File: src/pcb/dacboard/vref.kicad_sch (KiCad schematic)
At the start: 48 parts, among them J1 Screw_Terminal_01x03, J2 Screw_Terminal_01x02, U1 LTC6655CHMS8-2.5_PBF, U2 LTC6655CHMS8-2.5_PBF, U3 LTC6655CHMS8-2.5_PBF, U4 LTC6655CHMS8-2.5_PBF, U5 LTC6655CHMS8-2.5_PBF, U6 LTC6655CHMS8-2.5_PBF, U7 LTC6655CHMS8-2.5_PBF, U8 LTC6655CHMS8-2.5_PBF, U9 AD8676xR

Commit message: dacboard routing
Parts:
- C1, C11, C13, C15, C3, C5, C7, C9: footprint (none) -> Capacitor_SMD:C_0402_1005Metric_Pad0.74x0.62mm_HandSolder
- C10, C12, C14, C16, C2, C4, C6, C8: footprint (none) -> Capacitor_SMD:C_0603_1608Metric_Pad1.08x0.95mm_HandSolder
- C17, C18, C19, C20, C21: footprint (none) -> Capacitor_SMD:C_0805_2012Metric
- J1: footprint (none) -> TerminalBlock_Phoenix:TerminalBlock_Phoenix_MKDS-1,5-3-5.08_1x03_P5.08mm_Horizontal
- J2: footprint (none) -> TerminalBlock_4Ucon:TerminalBlock_4Ucon_1x02_P3.50mm_Horizontal
- R1, R2, R3, R4, R5, R6, R7, R8: footprint (none) -> Resistor_SMD:R_0805_2012Metric_Pad1.20x1.40mm_HandSolder
- R10, R9: footprint LT5400BCMS8E-7_PBF:SOP65P490X110-9N -> Package_SO:MSOP-8-1EP_3x3mm_P0.65mm_EP1.68x1.88mm
- R11, R12, R13, R14: footprint (none) -> Resistor_SMD:R_0805_2012Metric
- R15, R40: footprint (none) -> Resistor_THT:R_Axial_DIN0309_L9.0mm_D3.2mm_P12.70mm_Horizontal
- U1, U2, U3, U4, U5, U6, U7, U8: footprint LTC6655CHMS8-2.5_PBF:SOP65P490X110-8N -> Package_LCC:Analog_LCC-8_5x5mm_P1.27mm
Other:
- moved on the sheet: J2

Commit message: analog side layout
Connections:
- net AGND: now also U9.5 (+); no longer U9.3 (+)
- net at C17.1, R1.2, R2.2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: now also U9.3 (+); no longer U9.5 (+)
- net at R10.1, R10.2: now also U9.2 (-); no longer U9.6 (-)
- net at R10.8, R13.1: now also U9.1; no longer U9.7
- net at R11.1, R9.8: now also U9.7; no longer U9.1
- net at R9.1, R9.2, R9.3: now also U9.6 (-); no longer U9.2 (-)
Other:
- moved on the sheet: U9A, U9B
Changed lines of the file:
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@@
 	)
 	(junction
+		(at 224.79 85.09)
+		(diameter 0)
+		(color 0 0 0 0)
+	)
+	(junction
 		(at 184.15 127)
 		(diameter 0)
@@
 	)
 	(junction
-		(at 224.79 129.54)
-		(diameter 0)
-		(color 0 0 0 0)
-	)
-	(junction
 		(at 30.48 52.07)
 		(diameter 0)
@@
 	)
 	(junction
-		(at 224.79 85.09)
-		(diameter 0)
-		(color 0 0 0 0)
-	)
-	(junction
 		(at 133.35 156.21)
 		(diameter 0)
@@
 	)
 	(junction
+		(at 224.79 129.54)
+		(diameter 0)
+		(color 0 0 0 0)
+	)
+	(junction
 		(at 138.43 114.3)
 		(diameter 0)
@@
 	(wire
 		(pts
-			(xy 196.85 87.63) (xy 201.93 87.63)
-		)
-		(stroke
-			(width 0)
-			(type default)
-		)
-	)
-	(wire
-		(pts
 			(xy 87.63 138.43) (xy 97.79 138.43)
 		)
@@
 	(wire
 		(pts
+			(xy 196.85 132.08) (xy 203.2 132.08)
+		)
+		(stroke
+			(width 0)
+			(type default)
+		)
+	)
+	(wire
+		(pts
 			(xy 133.35 119.38) (xy 133.35 121.92)
 		)
@@
 	(wire
 		(pts
-			(xy 201.93 132.08) (xy 196.85 132.08)
-		)
-		(stroke
-			(width 0)
-			(type default)
-		)
-	)
-	(wire
-		(pts
 			(xy 184.15 82.55) (xy 184.15 91.44)
 		)
@@
 	(wire
 		(pts
-			(xy 184.15 127) (xy 201.93 127)
-		)
-		(stroke
-			(width 0)
-			(type default)
-		)
-	)
-	(wire
-		(pts
 			(xy 184.15 109.22) (xy 184.15 115.57)
 		)
@@
 	(wire
 		(pts
-			(xy 217.17 85.09) (xy 224.79 85.09)
-		)
-		(stroke
-			(width 0)
-			(type default)
-		)
-	)
-	(wire
-		(pts
 			(xy 71.12 113.03) (xy 66.04 113.03)
 		)
@@
 	(wire
 		(pts
+			(xy 218.44 85.09) (xy 224.79 85.09)
+		)
+		(stroke
+			(width 0)
+			(type default)
+		)
+	)
+	(wire
+		(pts
 			(xy 66.04 87.63) (xy 66.04 90.17)
 		)
@@
 	(wire
 		(pts
+			(xy 196.85 87.63) (xy 203.2 87.63)
+		)
+		(stroke
+			(width 0)
+			(type default)
+		)
+	)
+	(wire
+		(pts
 			(xy 30.48 107.95) (xy 30.48 113.03)
 		)
@@
 	(wire
 		(pts
-			(xy 224.79 99.06) (xy 219.71 99.06)
+			(xy 184.15 127) (xy 203.2 127)
 		)
 		(stroke
@@
 	(wire
 		(pts
-			(xy 71.12 46.99) (xy 72.39 46.99)
+			(xy 224.79 99.06) (xy 219.71 99.06)
 		)
 		(stroke
@@
 	(wire
 		(pts
-			(xy 20.32 46.99) (xy 30.48 46.99)
+			(xy 71.12 46.99) (xy 72.39 46.99)
 		)
 		(stroke
@@
 	(wire
 		(pts
-			(xy 224.79 129.54) (xy 217.17 129.54)
+			(xy 218.44 129.54) (xy 224.79 129.54)
 		)
 		(stroke
@@
 	(wire
 		(pts
-			(xy 224.79 102.87) (xy 224.79 115.57)
+			(xy 20.32 46.99) (xy 30.48 46.99)
 		)
 		(stroke
@@
 	(wire
 		(pts
-			(xy 193.04 82.55) (xy 201.93 82.55)
+			(xy 224.79 102.87) (xy 224.79 115.57)
 		)
 		(stroke
@@
 	(wire
 		(pts
+			(xy 193.04 82.55) (xy 203.2 82.55)
+		)
+		(stroke
+			(width 0)
+			(type default)
+		)
+	)
+	(wire
+		(pts
 			(xy 87.63 77.47) (xy 97.79 77.47)
 		)
@@
 	(symbol
 		(lib_id "Amplifier_Operational:AD8676xR")
-		(at 209.55 129.54 0)
+		(at 210.82 85.09 0)
 		(unit 2)
 		(exclude_from_sim no)
@@
 		(fields_autoplaced yes)
 		(property "Reference" "U9"
-			(at 209.55 119.38 0)
+			(at 210.82 74.93 0)
 			(effects
 				(font
@@
 		)
 		(property "Value" "AD8676xR"
-			(at 209.55 121.92 0)
+			(at 210.82 77.47 0)
 			(effects
 				(font
@@
 		)
 		(property "Footprint" "Package_SO:SOIC-8_3.9x4.9mm_P1.27mm"
-			(at 212.09 129.54 0)
+			(at 213.36 85.09 0)
 			(effects
 				(font
@@
 		)
 		(property "Datasheet" "https://www.analog.com/media/en/technical-documentation/data-sheets/AD8676.pdf"
-			(at 215.9 125.73 0)
+			(at 217.17 81.28 0)
 			(effects
 				(font
@@
 		)
 		(property "Description" "Dual operational amplifier, Ultra-precision, 36V, Rail-to-rail output, SOIC-8"
-			(at 209.55 129.54 0)
+			(at 210.82 85.09 0)
 			(effects
 				(font
@@
 	(symbol
 		(lib_id "Amplifier_Operational:AD8676xR")
-		(at 209.55 85.09 0)
+		(at 210.82 129.54 0)
 		(unit 1)
 		(exclude_from_sim no)
@@
 		(fields_autoplaced yes)
 		(property "Reference" "U9"
-			(at 209.55 74.93 0)
+			(at 210.82 119.38 0)
 			(effects
 				(font
@@
 		)
 		(property "Value" "AD8676xR"
-			(at 209.55 77.47 0)
+			(at 210.82 121.92 0)
 			(effects
 				(font
@@
 		)
 		(property "Footprint" "Package_SO:SOIC-8_3.9x4.9mm_P1.27mm"
-			(at 212.09 85.09 0)
+			(at 213.36 129.54 0)
 			(effects
 				(font
@@
 		)
 		(property "Datasheet" "https://www.analog.com/media/en/technical-documentation/data-sheets/AD8676.pdf"
-			(at 215.9 81.28 0)
+			(at 217.17 125.73 0)
 			(effects
 				(font
@@
 		)
 		(property "Description" "Dual operational amplifier, Ultra-precision, 36V, Rail-to-rail output, SOIC-8"
-			(at 209.55 85.09 0)
+			(at 210.82 129.54 0)
 			(effects
 				(font

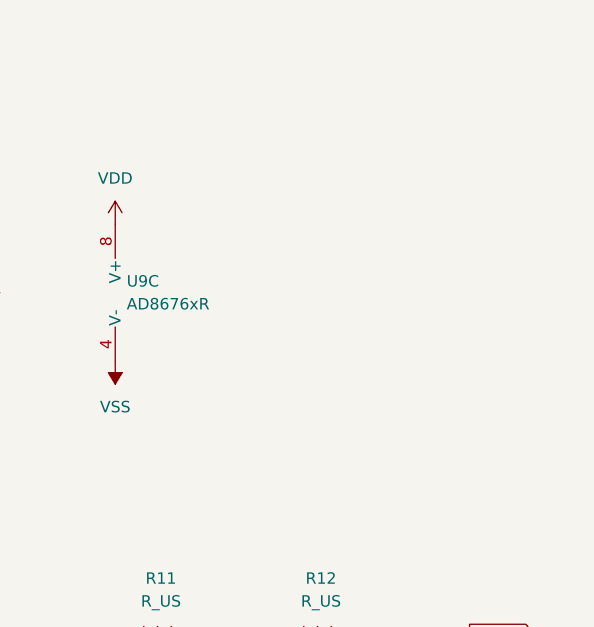
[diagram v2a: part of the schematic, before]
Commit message: low noise digital finished
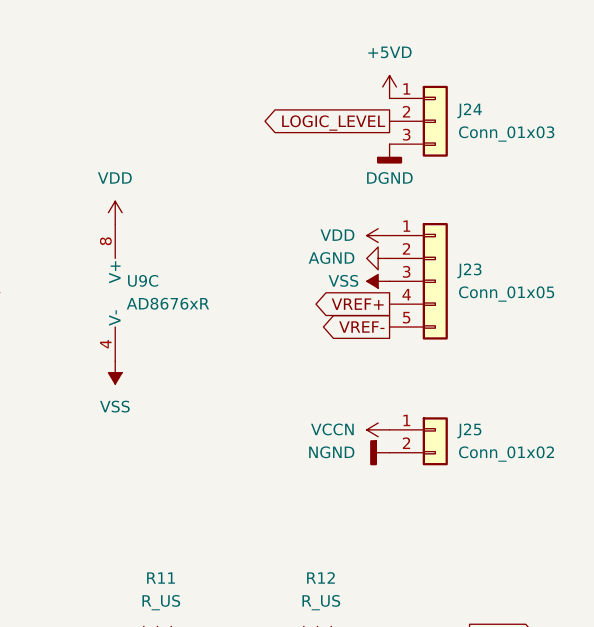
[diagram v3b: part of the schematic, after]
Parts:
- added J23: Conn_01x05, Connector_PinHeader_2.54mm:PinHeader_1x05_P2.54mm_Vertical, symbol Connector_Generic:Conn_01x05
- added J24: Conn_01x03, Connector_PinHeader_2.54mm:PinHeader_1x03_P2.54mm_Vertical, symbol Connector_Generic:Conn_01x03
- added J25: Conn_01x02, Connector_PinHeader_2.54mm:PinHeader_1x02_P2.54mm_Vertical, symbol Connector_Generic:Conn_01x02
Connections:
- net +5VD: now also J24.1 (Pin_1)
- net AGND: now also J23.2 (Pin_2)
- net DGND: now also J24.3 (Pin_3)
- net LOGIC_LEVEL: now also J24.2 (Pin_2)
- net VDD: now also J23.1 (Pin_1)
- net VREF+: now also J23.4 (Pin_4)
- net VREF-: now also J23.5 (Pin_5)
- net VSS: now also J23.3 (Pin_3)
- new net NGND: J25.2 (Pin_2)
- new net VCCN: J25.1 (Pin_1)

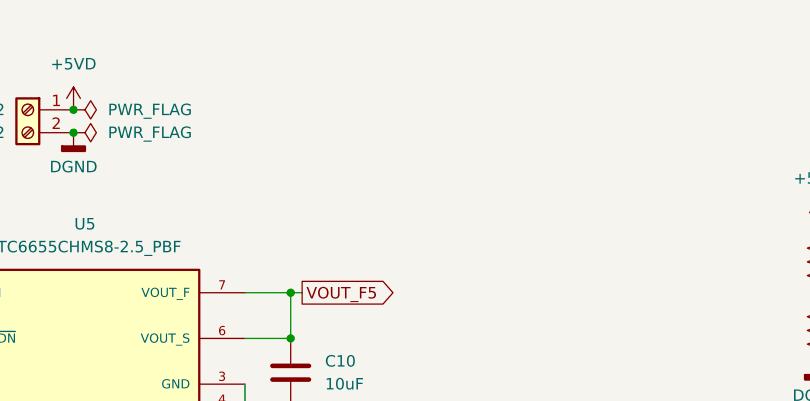
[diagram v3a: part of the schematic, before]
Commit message: finished routing fpga connections
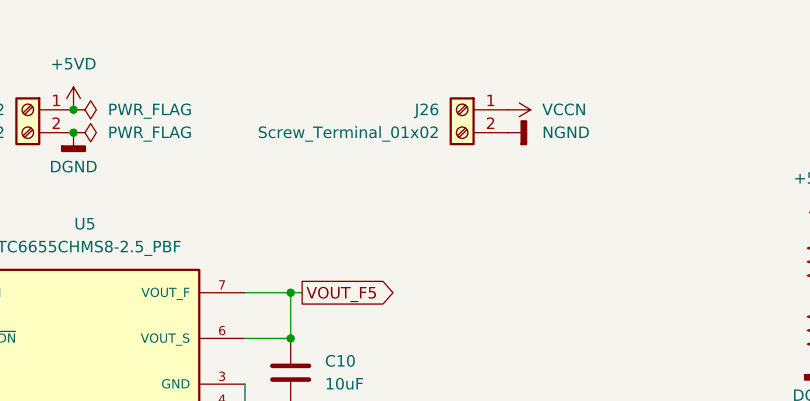
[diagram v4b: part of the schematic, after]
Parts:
- added J26: Screw_Terminal_01x02, TerminalBlock_4Ucon:TerminalBlock_4Ucon_1x02_P3.50mm_Horizontal, symbol Connector:Screw_Terminal_01x02
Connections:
- net NGND: now also J26.2 (Pin_2)
- net VCCN: now also J26.1 (Pin_1)
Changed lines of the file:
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@@
 	)
 	(symbol
+		(lib_id "power:GNDD")
+		(at 162.56 29.21 90)
+		(unit 1)
+		(exclude_from_sim no)
+		(in_bom yes)
+		(on_board yes)
+		(dnp no)
+		(fields_autoplaced yes)
+		(property "Reference" "#PWR0509"
+			(at 168.91 29.21 0)
+			(effects
+				(font
+					(size 1.27 1.27)
+				)
+				(hide yes)
+			)
+		)
+		(property "Value" "NGND"
+			(at 166.37 29.2099 90)
+			(effects
+				(font
+					(size 1.27 1.27)
+				)
+				(justify right)
+			)
+		)
+		(property "Footprint" ""
+			(at 162.56 29.21 0)
+			(effects
+				(font
+					(size 1.27 1.27)
+				)
+				(hide yes)
+			)
+		)
+		(property "Datasheet" ""
+			(at 162.56 29.21 0)
+			(effects
+				(font
+					(size 1.27 1.27)
+				)
+				(hide yes)
+			)
+		)
+		(property "Description" "Power symbol creates a global label with name \"GNDD\" , digital ground"
+			(at 162.56 29.21 0)
+			(effects
+				(font
+					(size 1.27 1.27)
+				)
+				(hide yes)
+			)
+		)
+		(pin "1"
+		)
+		(instances
+			(project "dacboard"
+				(path "/35cb74e4-0f64-454b-9b50-bfac13ed28a5/40dec0c3-ad5f-493b-813b-faaee90d807a"
+					(reference "#PWR0509")
+					(unit 1)
+				)
+			)
+		)
+	)
+	(symbol
 		(lib_id "power:GND")
 		(at 138.43 121.92 0)
@@
 	)
 	(symbol
+		(lib_id "power:VCC")
+		(at 162.56 26.67 270)
+		(mirror x)
+		(unit 1)
+		(exclude_from_sim no)
+		(in_bom yes)
+		(on_board yes)
+		(dnp no)
+		(property "Reference" "#PWR0508"
+			(at 158.75 26.67 0)
+			(effects
+				(font
+					(size 1.27 1.27)
+				)
+				(hide yes)
+			)
+		)
+		(property "Value" "VCCN"
+			(at 166.37 26.6699 90)
+			(effects
+				(font
+					(size 1.27 1.27)
+				)
+				(justify left)
+			)
+		)
+		(property "Footprint" ""
+			(at 162.56 26.67 0)
+			(effects
+				(font
+					(size 1.27 1.27)
+				)
+				(hide yes)
+			)
+		)
+		(property "Datasheet" ""
+			(at 162.56 26.67 0)
+			(effects
+				(font
+					(size 1.27 1.27)
+				)
+				(hide yes)
+			)
+		)
+		(property "Description" "Power symbol creates a global label with name \"VCC\""
+			(at 162.56 26.67 0)
+			(effects
+				(font
+					(size 1.27 1.27)
+				)
+				(hide yes)
+			)
+		)
+		(pin "1"
+		)
+		(instances
+			(project "dacboard"
+				(path "/35cb74e4-0f64-454b-9b50-bfac13ed28a5/40dec0c3-ad5f-493b-813b-faaee90d807a"
+					(reference "#PWR0508")
+					(unit 1)
+				)
+			)
+		)
+	)
+	(symbol
 		(lib_id "power:GND")
 		(at 66.04 95.25 0)
@@
 					(unit 1)
 				)
+			)
+		)
+	)
+	(symbol
+		(lib_id "Connector:Screw_Terminal_01x02")
+		(at 157.48 26.67 0)
+		(mirror y)
+		(unit 1)
+		(exclude_from_sim no)
+		(in_bom yes)
+		(on_board yes)
+		(dnp no)
+		(property "Reference" "J26"
+			(at 154.94 26.6699 0)
+			(effects
+				(font
+					(size 1.27 1.27)
+				)
+				(justify left)
+			)
+		)
+		(property "Value" "Screw_Terminal_01x02"
+			(at 154.94 29.2099 0)
+			(effects
+				(font
+					(size 1.27 1.27)
+				)
+				(justify left)
+			)
+		)
+		(property "Footprint" "TerminalBlock_4Ucon:TerminalBlock_4Ucon_1x02_P3.50mm_Horizontal"
+			(at 157.48 26.67 0)
+			(effects
+				(font
+					(size 1.27 1.27)
+				)
+				(hide yes)
+			)
+		)
+		(property "Datasheet" "~"
+			(at 157.48 26.67 0)
+			(effects
+				(font
+					(size 1.27 1.27)
+				)
+				(hide yes)
+			)
+		)
+		(property "Description" "Generic screw terminal, single row, 01x02, script generated (kicad-library-utils/schlib/autogen/connector/)"
+			(at 157.48 26.67 0)
+			(effects
+				(font
+					(size 1.27 1.27)
+				)
+				(hide yes)
+			)
+		)
+		(pin "1"
+		)
+		(pin "2"
+		)
+		(instances
+			(project "dacboard"
+				(path "/35cb74e4-0f64-454b-9b50-bfac13ed28a5/40dec0c3-ad5f-493b-813b-faaee90d807a"
+					(reference "J26")
+					(unit 1)
+				)

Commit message: dacboard finished
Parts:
- added R41: R_US, Resistor_THT:R_Axial_DIN0309_L9.0mm_D3.2mm_P20.32mm_Horizontal, symbol Device:R_US
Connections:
- net AGND: now also R41.1
- net DGND: now also R41.2
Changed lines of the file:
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@@
 	(symbol
 		(lib_id "Device:R_US")
+		(at 165.1 46.99 0)
+		(unit 1)
+		(exclude_from_sim no)
+		(in_bom yes)
+		(on_board yes)
+		(dnp no)
+		(fields_autoplaced yes)
+		(property "Reference" "R41"
+			(at 167.64 45.7199 0)
+			(effects
+				(font
+					(size 1.27 1.27)
+				)
+				(justify left)
+			)
+		)
+		(property "Value" "R_US"
+			(at 167.64 48.2599 0)
+			(effects
+				(font
+					(size 1.27 1.27)
+				)
+				(justify left)
+			)
+		)
+		(property "Footprint" "Resistor_THT:R_Axial_DIN0309_L9.0mm_D3.2mm_P20.32mm_Horizontal"
+			(at 166.116 47.244 90)
+			(effects
+				(font
+					(size 1.27 1.27)
+				)
+				(hide yes)
+			)
+		)
+		(property "Datasheet" "~"
+			(at 165.1 46.99 0)
+			(effects
+				(font
+					(size 1.27 1.27)
+				)
+				(hide yes)
+			)
+		)
+		(property "Description" "Resistor, US symbol"
+			(at 165.1 46.99 0)
+			(effects
+				(font
+					(size 1.27 1.27)
+				)
+				(hide yes)
+			)
+		)
+		(pin "1"
+		)
+		(pin "2"
+		)
+		(instances
+			(project ""
+				(path "/35cb74e4-0f64-454b-9b50-bfac13ed28a5/40dec0c3-ad5f-493b-813b-faaee90d807a"
+					(reference "R41")
+					(unit 1)
+				)
+			)
+		)
+	)
+	(symbol
+		(lib_id "Device:R_US")
 		(at 180.34 127 90)
 		(unit 1)
@@
 	)
 	(symbol
+		(lib_id "power:GNDD")
+		(at 165.1 50.8 0)
+		(unit 1)
+		(exclude_from_sim no)
+		(in_bom yes)
+		(on_board yes)
+		(dnp no)
+		(fields_autoplaced yes)
+		(property "Reference" "#PWR0542"
+			(at 165.1 57.15 0)
+			(effects
+				(font
+					(size 1.27 1.27)
+				)
+				(hide yes)
+			)
+		)
+		(property "Value" "DGND"
+			(at 165.1 54.61 0)
+			(effects
+				(font
+					(size 1.27 1.27)
+				)
+			)
+		)
+		(property "Footprint" ""
+			(at 165.1 50.8 0)
+			(effects
+				(font
+					(size 1.27 1.27)
+				)
+				(hide yes)
+			)
+		)
+		(property "Datasheet" ""
+			(at 165.1 50.8 0)
+			(effects
+				(font
+					(size 1.27 1.27)
+				)
+				(hide yes)
+			)
+		)
+		(property "Description" "Power symbol creates a global label with name \"GNDD\" , digital ground"
+			(at 165.1 50.8 0)
+			(effects
+				(font
+					(size 1.27 1.27)
+				)
+				(hide yes)
+			)
+		)
+		(pin "1"
+		)
+		(instances
+			(project "dacboard"
+				(path "/35cb74e4-0f64-454b-9b50-bfac13ed28a5/40dec0c3-ad5f-493b-813b-faaee90d807a"
+					(reference "#PWR0542")
+					(unit 1)
+				)
+			)
+		)
+	)
+	(symbol
 		(lib_id "power:GND")
 		(at 97.79 90.17 0)
@@
 					(unit 1)
 				)
+			)
+		)
+	)
+	(symbol
+		(lib_id "power:GND")
+		(at 165.1 43.18 180)
+		(unit 1)
+		(exclude_from_sim no)
+		(in_bom yes)
+		(on_board yes)
+		(dnp no)
+		(property "Reference" "#PWR0543"
+			(at 165.1 36.83 0)
+			(effects
+				(font
+					(size 1.27 1.27)
+				)
+				(hide yes)
+			)
+		)
+		(property "Value" "AGND"
+			(at 161.544 40.894 0)
+			(effects
+				(font
+					(size 1.27 1.27)
+				)
+			)
+		)
+		(property "Footprint" ""
+			(at 165.1 43.18 0)
+			(effects
+				(font
+					(size 1.27 1.27)
+				)
+				(hide yes)
+			)
+		)
+		(property "Datasheet" ""
+			(at 165.1 43.18 0)
+			(effects
+				(font
+					(size 1.27 1.27)
+				)
+				(hide yes)
+			)
+		)
+		(property "Description" "Power symbol creates a global label with name \"GND\" , ground"
+			(at 165.1 43.18 0)
+			(effects
+				(font
+					(size 1.27 1.27)
+				)
+				(hide yes)
+			)
+		)
+		(pin "1"
+		)
+		(instances
+			(project "dacboard"
+				(path "/35cb74e4-0f64-454b-9b50-bfac13ed28a5/40dec0c3-ad5f-493b-813b-faaee90d807a"
+					(reference "#PWR0543")
+					(unit 1)
+				)
